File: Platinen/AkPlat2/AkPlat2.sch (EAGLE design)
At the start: 18 parts, among them M1 22-23-2021, M2 22-23-2021, M3 22-23-2021, M4 22-23-2021

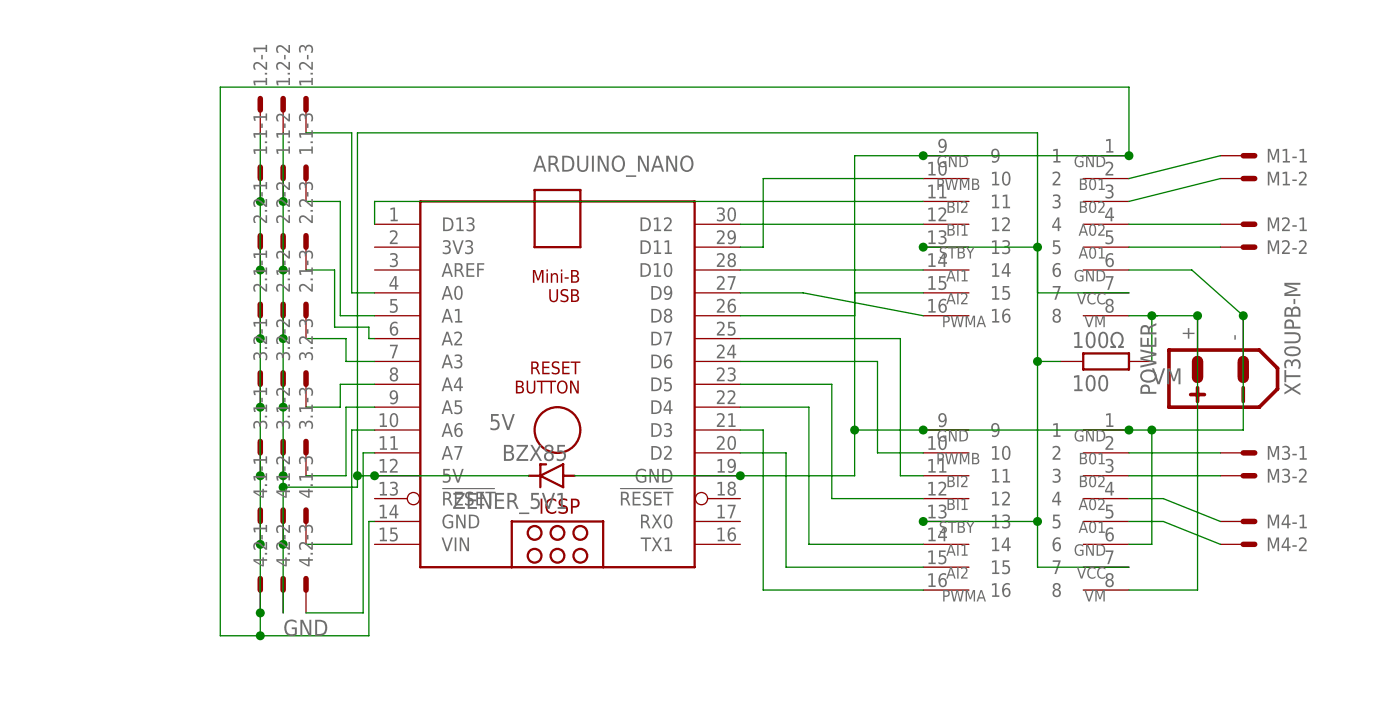
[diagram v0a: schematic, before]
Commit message: Motorcontroller Platine V3.0 finished
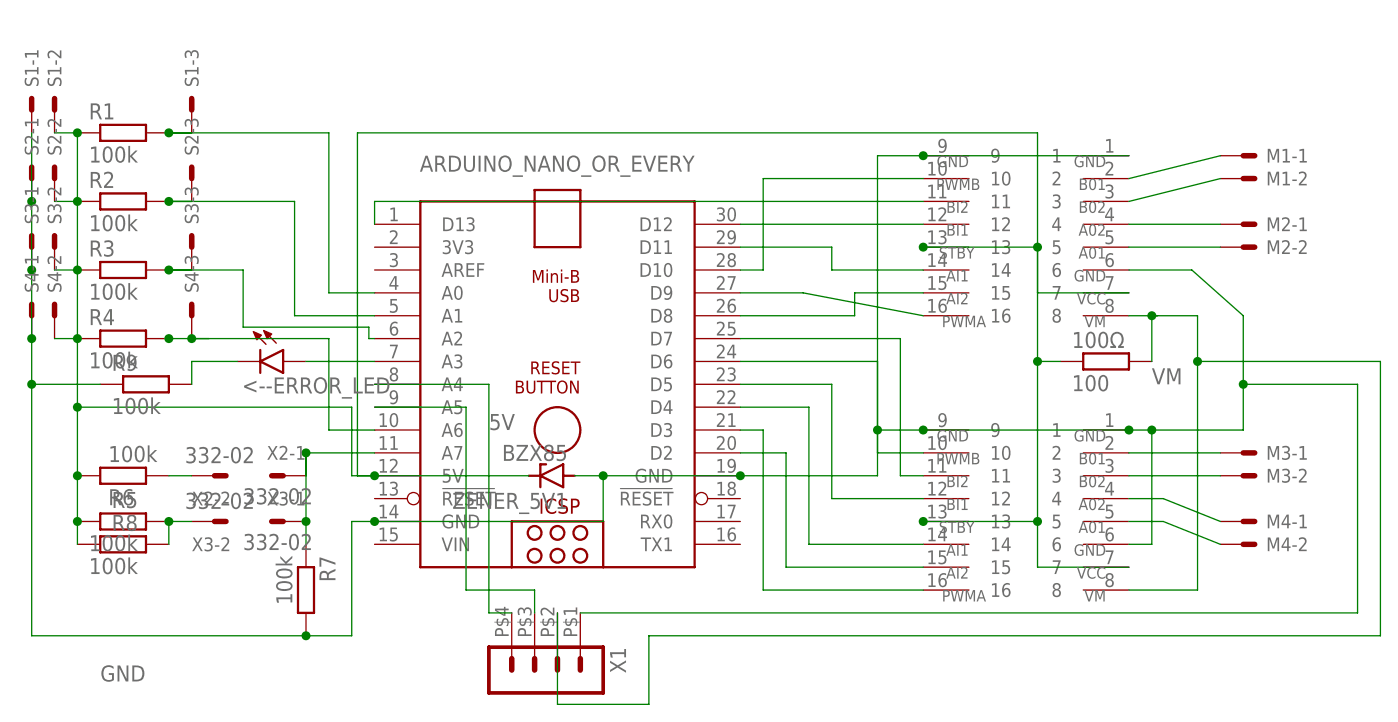
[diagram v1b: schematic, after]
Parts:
- removed 1.1, 1.2, 2.1, 2.2, 3.1, 3.2, 4.1, 4.2: 22-23-2031, con-molex:22-23-2031
- removed POWER: XT30UPB-M, amass:XT30UPB-M
- added <--ERROR_LED: (no value), led:LED3MM
- added R1, R2, R3, R4, R5, R6, R7, R8, R9: 100k, rcl:R-EU_R0402
- added S1, S2, S3, S4: 22-23-2031, con-molex:22-23-2031
- added X1: (no value), con-molex-micro-fit-3_0:HEADER_POS4_43045-0412
- added X2, X3: 332-02, con-garry:332-02
- renumbered ARDUINO_NANO to ARDUINO_NANO_OR_EVERY
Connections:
- removed net N$27: 4.1-3.S, ARDUINO_NANO_OR_EVERY.A6
- removed net N$30: 3.1-3.S, ARDUINO_NANO_OR_EVERY.A5
- removed net N$31: 3.2-3.S, ARDUINO_NANO_OR_EVERY.A4
- new net N$1: ARDUINO_NANO_OR_EVERY.A4, X1.4
- new net N$15: R6.1, X2-2.S
- new net N$2: ARDUINO_NANO_OR_EVERY.A5, X1.3
- new net N$24: R5.2, R8.2, X3-2.S
- new net N$25: <--ERROR_LED.A, ARDUINO_NANO_OR_EVERY.A3
- new net N$8: ARDUINO_NANO_OR_EVERY.A7, R7.1, X2-1.S, X3-1.S
- net 5V: now also R1.1, R2.1, R3.1, R4.1, R5.1, R6.2, R8.1, S1-2.S, S2-2.S, S3-2.S, S4-2.S; no longer 1.1-2.S, 1.2-2.S, 2.1-2.S, 2.2-2.S, 3.1-2.S, 3.2-2.S, 4.1-2.S, 4.2-2.S
- net GND: now also R7.2, R9.1, S1-1.S, S2-1.S, S3-1.S, S4-1.S, X1.1; no longer 1.1-1.S, 1.2-1.S, 2.1-1.S, 2.2-1.S, 3.1-1.S, 3.2-1.S, 4.1-1.S, 4.2-1.S, POWER.-
- net N$26: now also <--ERROR_LED.C, R9.2; no longer 4.2-3.S, ARDUINO_NANO_OR_EVERY.A7
- net N$32: now also ARDUINO_NANO_OR_EVERY.A6, R4.2, S4-3.S; no longer 2.1-3.S, ARDUINO_NANO_OR_EVERY.A3
- net N$33: now also R3.2, S3-3.S; no longer 2.2-3.S
- net N$34: now also R2.2, S2-3.S; no longer 1.1-3.S
- net N$35: now also R1.2, S1-3.S; no longer 1.2-3.S
- net N$6: now also ARDUINO_NANO_OR_EVERY.D10; no longer ARDUINO_NANO_OR_EVERY.D11
- net N$7: now also ARDUINO_NANO_OR_EVERY.D11; no longer ARDUINO_NANO_OR_EVERY.D10
- net VM: now also X1.2; no longer POWER.+
